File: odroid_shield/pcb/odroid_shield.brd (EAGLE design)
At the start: 83 x 48 mm, 69 parts, among them J1 AVRISP6_COMPACT, J4 ODROID_J4, U1 SINGLE-BIT_BUS_TRANSCEIVER, U10 ABM8G, U2 SINGLE-BIT_BUS_TRANSCEIVER, U3 ST1S10, U4 ATMEGA644P-20AU, U5 TS5205, U6 TCA9517MSOP8, U7 MP33926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

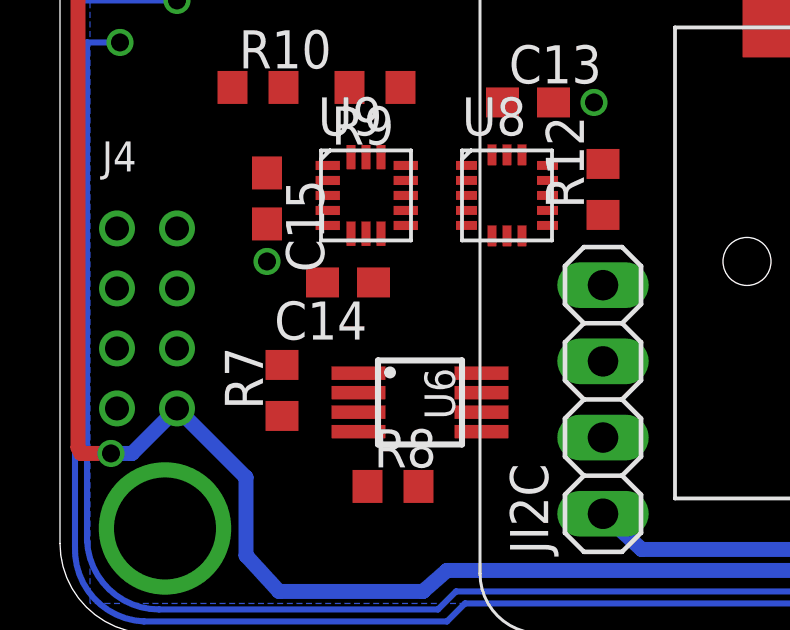
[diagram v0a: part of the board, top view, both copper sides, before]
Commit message: odroid_shield: Connect up the 33926's status pin to the AVR.
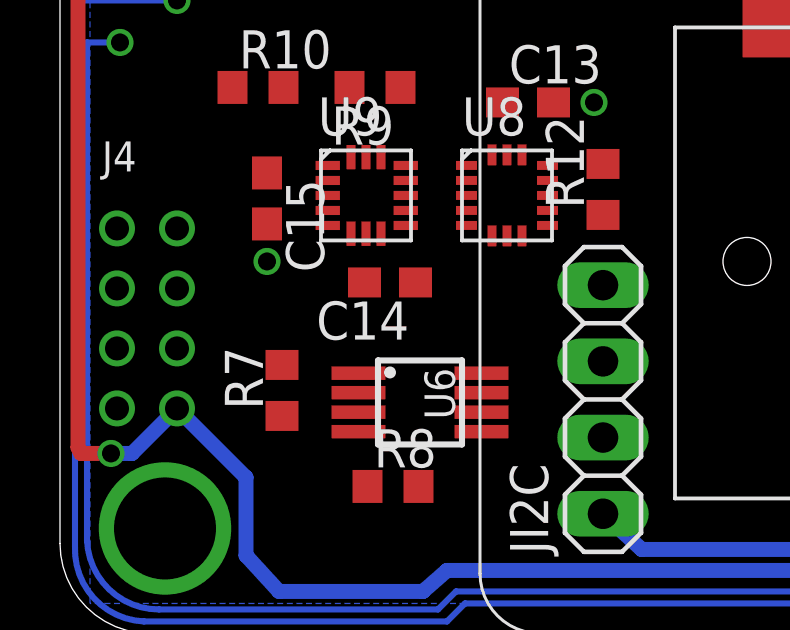
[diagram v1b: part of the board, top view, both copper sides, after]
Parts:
- moved C14 1.40 mm to (11.0, 11.7)
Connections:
- removed net N$29: R11.2, U4.24
- new net MOTOR_SF: R5.1, U4.24, U7.21
- net N$17: now also R11.2, U4.26; no longer R5.1, U7.21
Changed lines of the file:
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@@
 </element>
 <element name="U9" library="odroid_shield" package="QFN16" value="MMA8451Q" x="10.2" y="14.6"/>
-<element name="C14" library="rcl" package="C0603" value=".1uF" x="9.6" y="11.7" smashed="yes" rot="R180">
-<attribute name="NAME" x="10.235" y="11.065" size="1.27" layer="25" rot="R180"/>
+<element name="C14" library="rcl" package="C0603" value=".1uF" x="11" y="11.7" smashed="yes" rot="R180">
+<attribute name="NAME" x="11.635" y="11.065" size="1.27" layer="25" rot="R180"/>
 </element>
 <element name="C15" library="rcl" package="C0603" value=".1uF" x="6.9" y="14.5" smashed="yes" rot="R270">
@@
 <wire x1="38.8" y1="28.2" x2="38.8" y2="29" width="0" layer="19" extent="1-1"/>
 <wire x1="45.8" y1="30.6" x2="44.1" y2="30" width="0" layer="19" extent="1-1"/>
-<wire x1="8.75" y1="11.7" x2="6.9" y2="12.4" width="0" layer="19" extent="1-1"/>
-<wire x1="8.925" y1="13.6" x2="8.75" y2="11.7" width="0" layer="19" extent="1-1"/>
+<wire x1="10.15" y1="11.7" x2="6.9" y2="12.4" width="0" layer="19" extent="1-1"/>
+<wire x1="8.925" y1="13.6" x2="10.15" y2="11.7" width="0" layer="19" extent="1-1"/>
 <wire x1="11.525" y1="14.1" x2="8.925" y2="13.6" width="0" layer="19" extent="1-1"/>
 <wire x1="11.525" y1="15.1" x2="11.525" y2="14.1" width="0" layer="19" extent="1-1"/>
 <wire x1="13.55" y1="13.6" x2="11.525" y2="14.1" width="0" layer="19" extent="1-1"/>
 <wire x1="15.4" y1="13.25" x2="13.55" y2="13.6" width="0" layer="19" extent="1-1"/>
-<wire x1="9.95" y1="6.725" x2="8.75" y2="11.7" width="0" layer="19" extent="1-1"/>
+<wire x1="9.95" y1="6.725" x2="10.15" y2="11.7" width="0" layer="19" extent="1-1"/>
 <wire x1="15.8404" y1="34.7" x2="20.55" y2="36.8" width="0" layer="19" extent="1-16"/>
 <wire x1="44.45" y1="38.9" x2="44.1" y2="32.4" width="0" layer="19" extent="1-1"/>
@@
 <wire x1="45.55" y1="24.5" x2="44.7" y2="27.1" width="0" layer="19" extent="1-1"/>
 </signal>
-<signal name="N$17">
+<signal name="MOTOR_SF">
 <contactref element="R5" pad="1"/>
 <contactref element="U7" pad="21"/>
+<contactref element="U4" pad="24"/>
 <wire x1="38.8" y1="30.6" x2="41.85" y2="36.5" width="0" layer="19" extent="1-1"/>
+<wire x1="4.3596" y1="37.9004" x2="38.8" y2="30.6" width="0" layer="19" extent="1-1"/>
 </signal>
 <signal name="MOTOR_FB">
@@
 <wire x1="14.05" y1="6.725" x2="18.1" y2="3.99" width="0" layer="19" extent="1-1"/>
 <wire x1="14.05" y1="8.675" x2="14.05" y2="6.725" width="0" layer="19" extent="1-1"/>
-<wire x1="10.45" y1="11.7" x2="14.05" y2="8.675" width="0" layer="19" extent="1-1"/>
-<wire x1="10.2" y1="13.325" x2="10.45" y2="11.7" width="0" layer="19" extent="1-1"/>
+<wire x1="11.85" y1="11.7" x2="14.05" y2="8.675" width="0" layer="19" extent="1-1"/>
+<wire x1="10.2" y1="13.325" x2="11.85" y2="11.7" width="0" layer="19" extent="1-1"/>
 <wire x1="10.7" y1="15.875" x2="10.2" y2="13.325" width="0" layer="19" extent="1-1"/>
 <wire x1="8.925" y1="15.6" x2="10.7" y2="15.875" width="0" layer="19" extent="1-1"/>
@@
 <wire x1="13.6" y1="23.85" x2="15.6" y2="23.75" width="0" layer="19" extent="1-1"/>
 </signal>
-<signal name="N$29">
-<contactref element="R11" pad="2"/>
-<contactref element="U4" pad="24"/>
-<wire x1="4.3596" y1="37.9004" x2="13.6" y2="25.55" width="0" layer="19" extent="1-1"/>
-</signal>
 <signal name="N$32">
 <contactref element="U10" pad="1"/>
@@
 <wire x1="2.1" y1="31.65" x2="4.3596" y2="33.9126" width="0" layer="19" extent="1-1"/>
 </signal>
+<signal name="N$17">
+<contactref element="R11" pad="2"/>
+<contactref element="U4" pad="26"/>
+<wire x1="4.3596" y1="36.3002" x2="13.6" y2="25.55" width="0" layer="19" extent="1-1"/>
+</signal>
 </signals>

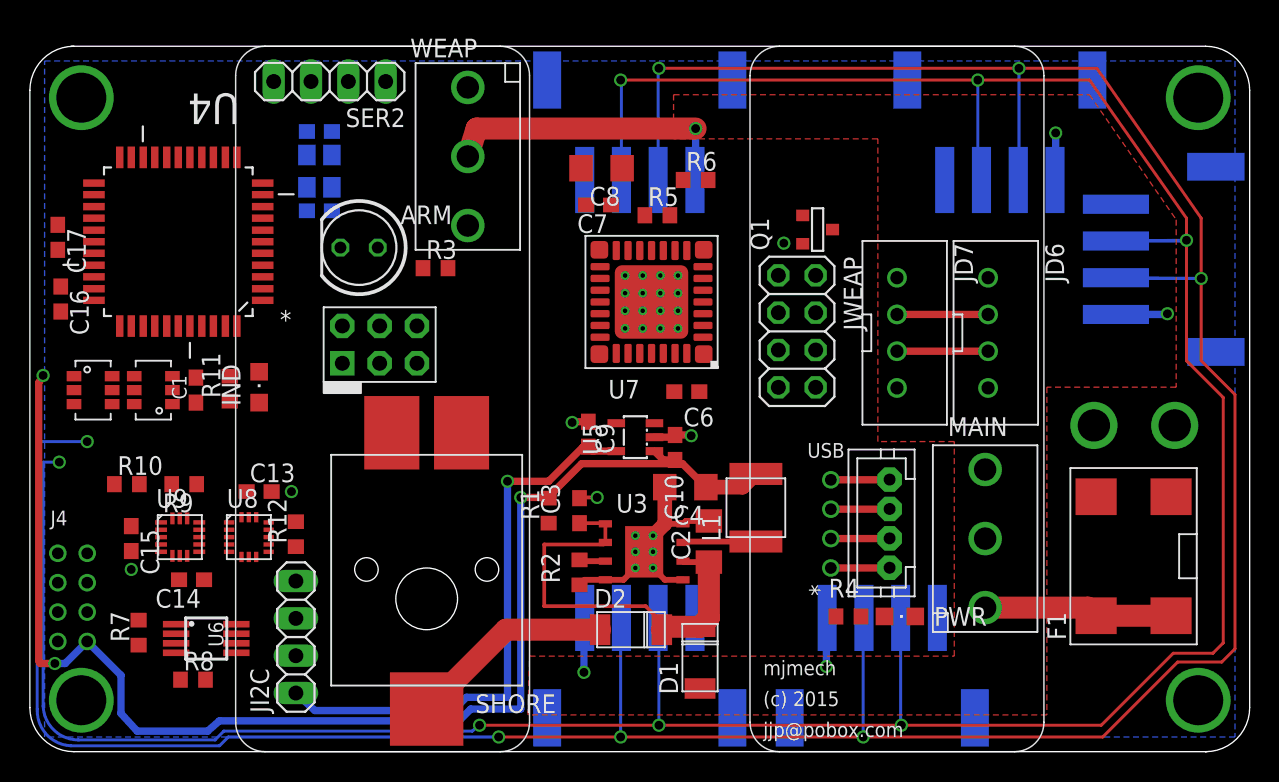
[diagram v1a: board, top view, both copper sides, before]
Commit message: odroid_shield: More progress on board.  Weapon fully routed, and I believe autoroute + some tweaks now gets a fully routable board.
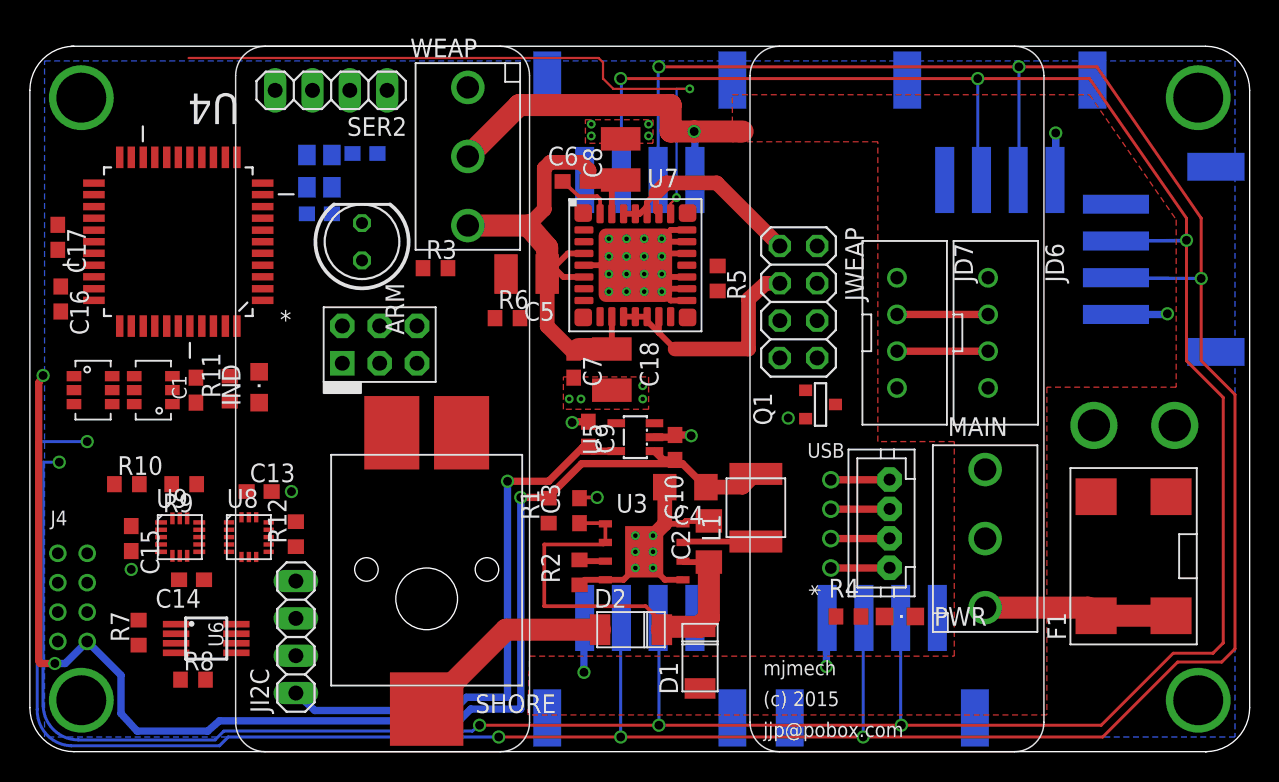
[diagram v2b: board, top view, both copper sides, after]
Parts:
- added C18, C5: 22uF 16V, rcl:C1210
- C8: value 10uF 16V -> 22uF 16V; device rcl:C1206 -> rcl:C1210
- moved C6 16.2 mm to (37.1, 38.8), turned to 180 degrees
- moved R6 15.9 mm to (32.5, 29.5)
- moved Q1 11.9 mm to (53.8, 23.6)
- moved C7 11.0 mm to (37.0, 26.3), turned to 270 degrees
- moved R5 5.94 mm to (46.8, 32.2), turned to 270 degrees
- moved C11 3.44 mm to (22.8, 40.7), turned to 180 degrees
- moved U7 2.73 mm to (41.2, 33.1), turned to 0 degrees
- moved JWEAP 2.00 mm to (52.3, 30.6)
- moved C8 1.43 mm to (40.2, 40.3), turned to 90 degrees
- moved SER2 0.61 mm to (20.5, 45.0)
- moved ARM 0.45 mm to (22.6, 34.7), turned to 90 degrees
- moved C12 0.20 mm to (19.7, 36.6)
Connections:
- removed net MOTOR_D2: U4.22, U7.16
- net +5V: now also U7.16
- net GND: now also C18.2, C5.2
- net N$12: now also U7.27, U7.28, U7.29, U7.30; no longer U7.12, U7.13, U7.14, U7.15
- net N$14: now also U7.12, U7.13, U7.14, U7.15; no longer U7.27, U7.28, U7.29, U7.30
- net N$15: now also C18.1, C5.1
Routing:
- net MOTOR_D1: track 0.00 -> 45.2 mm, vias 0 -> 2
- net N$15: track 0.00 -> 37.7 mm
- net N$14: track 0.00 -> 16.6 mm
- net N$12: track 0.00 -> 15.4 mm
- net GND: track 19.4 -> 32.4 mm, vias 6 -> 14
- net +8V: track 34.3 -> 39.2 mm
- net N$16: track 0.00 -> 4.02 mm
- added copper zone on layer 1, net GND

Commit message: odroid_shield: Route some more high power lines.
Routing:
- net N$7: track 0.00 -> 10.1 mm
- net GND: track 32.4 -> 39.7 mm, vias 14 -> 17
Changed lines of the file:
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@@
 <wire x1="44.7" y1="35.5" x2="43.6" y2="35.5" width="0.4" layer="1"/>
 <wire x1="43.6" y1="35.5" x2="43" y2="34.9" width="0.4" layer="1"/>
+<via x="23.4" y="18.6" extent="1-16" drill="0.3048"/>
+<via x="24.6" y="18.6" extent="1-16" drill="0.3048"/>
+<via x="25.8" y="18.6" extent="1-16" drill="0.3048"/>
+<wire x1="25.8" y1="18.6" x2="25.8" y2="20.525" width="0.4" layer="1"/>
+<wire x1="25.8" y1="20.525" x2="24.625" y2="21.7" width="0.4" layer="1"/>
 <wire x1="40.6" y1="32.5" x2="41.2" y2="33.1" width="0" layer="19" extent="1-1"/>
 <wire x1="41.8" y1="13.6" x2="41.2" y2="13.6" width="0" layer="19" extent="1-1"/>
@@
 <wire x1="32.4" y1="32.5" x2="37.7" y2="33.1" width="0" layer="19" extent="1-1"/>
 <wire x1="31.65" y1="29.5" x2="32.4" y2="32.5" width="0" layer="19" extent="1-1"/>
-<wire x1="24.625" y1="21.7" x2="26.34" y2="28.97" width="0" layer="19" extent="1-1"/>
 <wire x1="10.1" y1="28.9596" x2="15.8404" y2="34.7" width="0" layer="19" extent="1-1"/>
 <wire x1="11.3" y1="25.45" x2="10.1" y2="28.9596" width="0" layer="19" extent="1-1"/>
@@
 <wire x1="4.3596" y1="34.7" x2="1.9" y2="34.15" width="0" layer="19" extent="1-1"/>
 <wire x1="9.3126" y1="40.4404" x2="4.3596" y2="34.7" width="0" layer="19" extent="1-1"/>
+<wire x1="24.6" y1="18.6" x2="24.6" y2="20.3" width="0.4" layer="1"/>
+<wire x1="23.4" y1="18.6" x2="23.4" y2="20.6" width="0.4" layer="1"/>
 </signal>
 <signal name="N$2">
@@
 <contactref element="F1" pad="3"/>
 <contactref element="F1" pad="4"/>
-<wire x1="77.65" y1="17.35" x2="77.9" y2="22.2" width="0" layer="19" extent="1-1"/>
-<wire x1="72.55" y1="17.35" x2="77.65" y2="17.35" width="0" layer="19" extent="1-1"/>
+<wire x1="77.9" y1="22.2" x2="77.9" y2="17.6" width="1.5" layer="1"/>
+<wire x1="77.9" y1="17.6" x2="77.65" y2="17.35" width="1.5" layer="1"/>
+<wire x1="77.65" y1="17.35" x2="72.55" y2="17.35" width="1.5" layer="1"/>
 </signal>
 <signal name="N$11">

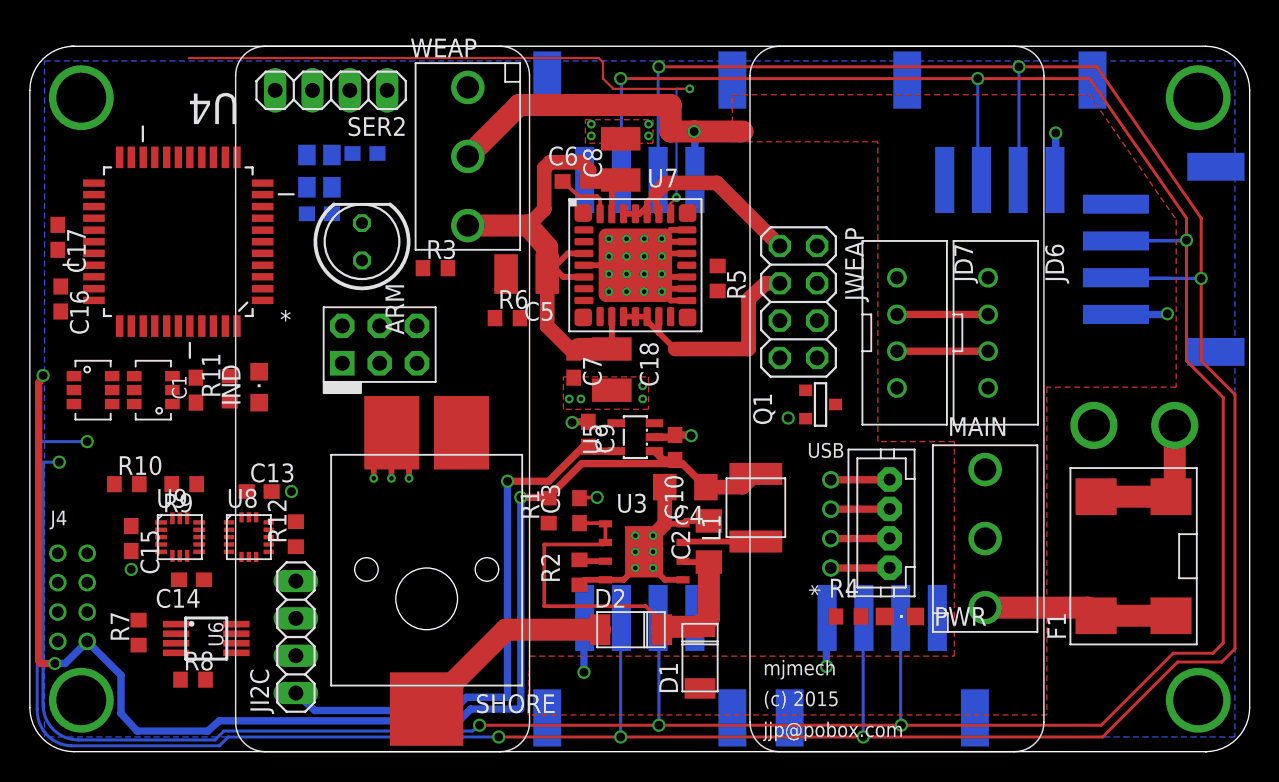
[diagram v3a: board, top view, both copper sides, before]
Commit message: odroid_shield: Add no-via regions under the MEMs parts.
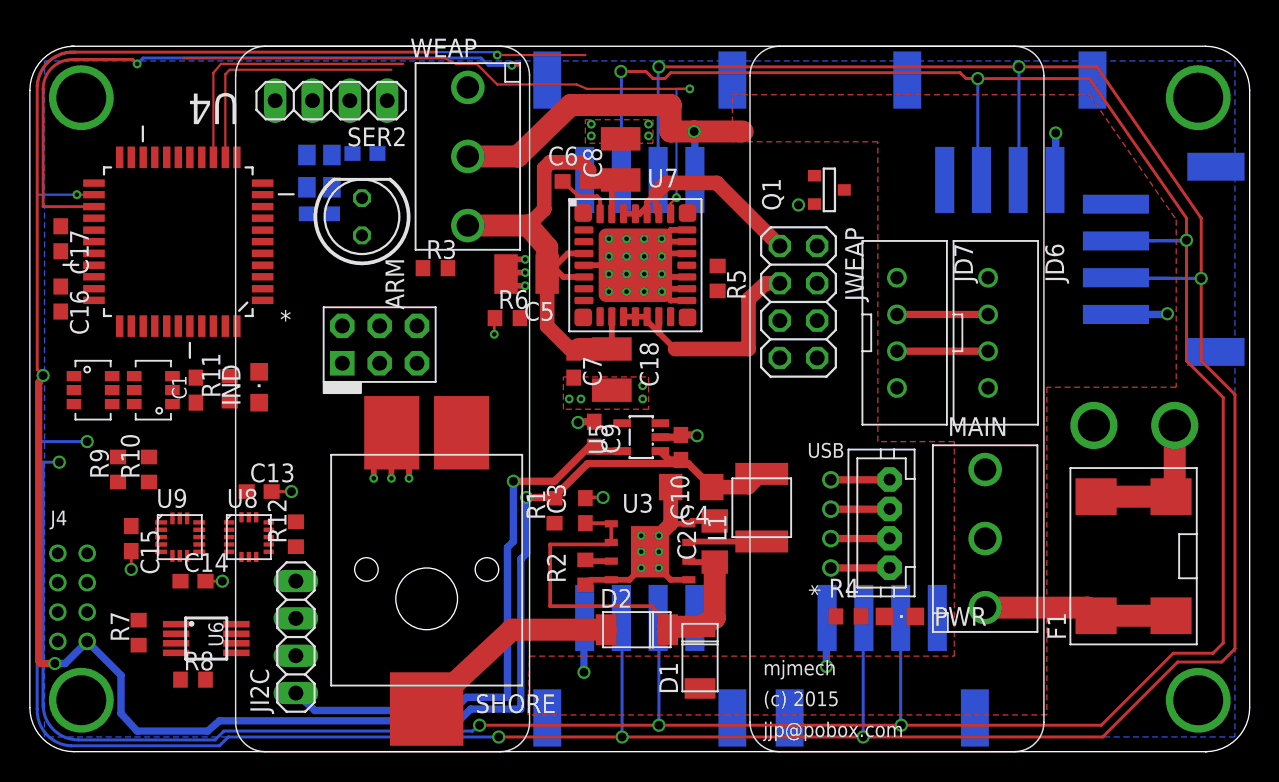
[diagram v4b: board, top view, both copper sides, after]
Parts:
- moved Q1 14.6 mm to (54.4, 38.2)
- moved R9 4.61 mm to (6.00, 19.2), turned to 90 degrees
- moved R10 1.80 mm to (8.10, 19.2), turned to 90 degrees
- moved ARM 1.70 mm to (22.6, 36.4)
- moved SER2 0.70 mm to (20.5, 44.3)
- moved R1 0.40 mm to (35.7, 16.4)
- moved U3 0.40 mm to (42.2, 13.6)
- moved C10 0.40 mm to (44.3, 20.7)
- moved C2 0.40 mm to (46.6, 14.3)
- moved C3 0.40 mm to (37.8, 16.4)
- moved C4 0.40 mm to (45.0, 18.0)
- moved C9 0.40 mm to (38.4, 21.6)
- moved D2 0.40 mm to (41.3, 8.30)
- moved L1 0.40 mm to (49.8, 16.6)
- moved R2 0.40 mm to (37.8, 12.2)
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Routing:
- net MOTOR_SF: track 0.00 -> 49.5 mm, vias 0 -> 2
- net +5V: track 91.8 -> 139.8 mm
- net LASER_EN: track 0.00 -> 45.2 mm, vias 0 -> 2
- net AGITATOR_PWM: track 0.00 -> 18.9 mm
- net AEG_PWM: track 0.00 -> 17.1 mm
- net GND: track 39.7 -> 48.3 mm, vias 17 -> 22
- net ODROID_RX_5V: track 219.6 -> 220.6 mm

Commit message: odroid_shield: More work on IMU.
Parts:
- moved R9 10.8 mm to (13.6, 11.5), turned to 0 degrees
- moved C14 8.40 mm to (11.3, 20.0)
- moved R10 6.77 mm to (11.9, 13.6), turned to 0 degrees
- moved R8 5.46 mm to (8.00, 9.40)
- moved U8 3.16 mm to (16.7, 17.2)
- moved U9 2.61 mm to (10.0, 17.2)
- moved C13 2.37 mm to (16.2, 20.0)
- moved C15 2.26 mm to (7.40, 16.7)
- moved R7 1.70 mm to (8.90, 7.30), turned to 0 degrees
- moved U6 1.25 mm to (13.1, 7.10), turned to 0 degrees
- moved R12 0.85 mm to (17.5, 14.2), turned to 0 degrees
- moved IND 0.22 mm to (15.5, 24.6)
- moved JI2C 0.10 mm to (18.2, 7.80)
- moved R11 0.10 mm to (13.6, 24.6)
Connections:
- net +3V3: now also U8.8
- net GND: no longer U8.8
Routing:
- net ODROID_SDA: track 0.00 -> 21.4 mm
- net ODROID_SCL: track 0.00 -> 20.2 mm
- net VCCIO: track 0.00 -> 14.8 mm
- net SYS_SCL: track 0.00 -> 14.4 mm
- net SYS_SDA: track 0.00 -> 9.57 mm
- net GND: track 48.3 -> 55.4 mm, vias 22 -> 28
- net +3V3: track 38.6 -> 44.1 mm
- net N$36: track 0.00 -> 1.39 mm
